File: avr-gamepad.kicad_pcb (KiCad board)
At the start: 2 copper layers, 26.2 x 48.3 mm, 33 parts, among them J1 Conn_01x08, J2 Conn_01x01, P1 USB_C_Plug_USB2.0, SW10 Up, SW11 Down, SW12 Left, SW13 Select, SW2 R, SW3 X, SW4 A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

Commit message: tweak silkscreen, add BOM
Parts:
- moved C8 0.07 mm to (140.8, 115.8), turned to 270 degrees
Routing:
- net Net-(C8-Pad1): track 2.63 -> 4.67 mm
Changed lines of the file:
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@@
     (thickness 0.1016)
     (drawings 40)
-    (tracks 455)
+    (tracks 460)
     (zones 0)
     (modules 33)
@@
     (at 151.462 125.016 180)
     (attr smd)
-    (fp_text reference SW6 (at 0 2.54) (layer F.SilkS)
+    (fp_text reference SW6 (at -0.176 2.08) (layer F.SilkS)
       (effects (font (size 1 1) (thickness 0.15)))
     )
@@
     (at 149.479 83.058 90)
     (attr smd)
-    (fp_text reference SW9 (at 0 -3.683 90) (layer B.SilkS)
+    (fp_text reference SW9 (at 3.4036 0.0254 180) (layer B.SilkS)
       (effects (font (size 1 1) (thickness 0.15)) (justify mirror))
     )
@@
     (tags capacitor)
     (attr smd)
-    (fp_text reference C1 (at 0 1.65) (layer B.SilkS)
+    (fp_text reference C1 (at -2.6876 -0.1384) (layer B.SilkS)
       (effects (font (size 1 1) (thickness 0.15)) (justify mirror))
     )
@@
     (tags capacitor)
     (attr smd)
-    (fp_text reference C2 (at 0 1.65) (layer B.SilkS)
+    (fp_text reference C2 (at -2.6876 -0.0124) (layer B.SilkS)
       (effects (font (size 1 1) (thickness 0.15)) (justify mirror))
     )
@@
     (tags capacitor)
     (attr smd)
-    (fp_text reference C3 (at 0 1.65) (layer B.SilkS)
+    (fp_text reference C3 (at -2.6576 0.0892) (layer B.SilkS)
       (effects (font (size 1 1) (thickness 0.15)) (justify mirror))
     )
@@
     (tags capacitor)
     (attr smd)
-    (fp_text reference C4 (at 0 1.65) (layer B.SilkS)
+    (fp_text reference C4 (at 0.3096 1.538) (layer B.SilkS)
       (effects (font (size 1 1) (thickness 0.15)) (justify mirror))
     )
@@
     (tags capacitor)
     (attr smd)
-    (fp_text reference C7 (at 2.667 -0.127 270) (layer B.SilkS)
+    (fp_text reference C7 (at 2.6388 0.0508 270) (layer B.SilkS)
       (effects (font (size 1 1) (thickness 0.15)) (justify mirror))
     )
@@
   )
   (module Capacitor_SMD:C_0805_2012Metric (layer B.Cu)
-    (at 140.716 115.746 90)
+    (at 140.7668 115.7963 270)
     (descr "Capacitor SMD 0805 (2012 Metric), square (rectangular) end terminal, IPC_7351 nominal, (Body size source: https://docs.google.com/spreadsheets/d/1BsfQQcO9C6DZCsRaXUlFlo91Tg2WpOkGARC1WS5S8t0/edit?usp=sharing), generated with kicad-footprint-generator")
     (tags capacitor)
     (attr smd)
-    (fp_text reference C8 (at 2.667 0 90) (layer B.SilkS)
+    (fp_text reference C8 (at 2.6693 -0.1016 90) (layer B.SilkS)
       (effects (font (size 1 1) (thickness 0.15)) (justify mirror))
     )
@@
     (fp_line (start -1 0.6) (end 1 0.6) (layer B.Fab) (width 0.1))
     (fp_line (start -1 -0.6) (end -1 0.6) (layer B.Fab) (width 0.1))
-    (pad 2 smd roundrect (at 0.9375 0 90) (size 0.975 1.4) (layers B.Cu B.Paste B.Mask) (roundrect_rratio 0.25)
-      (net 2 GND))
-    (pad 1 smd roundrect (at -0.9375 0 90) (size 0.975 1.4) (layers B.Cu B.Paste B.Mask) (roundrect_rratio 0.25)
+    (pad 2 smd roundrect (at 0.9375 0 270) (size 0.975 1.4) (layers B.Cu B.Paste B.Mask) (roundrect_rratio 0.25)
+      (net 2 GND))
+    (pad 1 smd roundrect (at -0.9375 0 270) (size 0.975 1.4) (layers B.Cu B.Paste B.Mask) (roundrect_rratio 0.25)
       (net 6 "Net-(C8-Pad1)"))
     (model ${KISYS3DMOD}/Capacitor_SMD.3dshapes/C_0805_2012Metric.wrl
@@
     (tags resistor)
     (attr smd)
-    (fp_text reference R1 (at -0.0381 -1.6891 180) (layer B.SilkS)
+    (fp_text reference R1 (at -0.1388 1.6528 180) (layer B.SilkS)
       (effects (font (size 1 1) (thickness 0.15)) (justify mirror))
     )
@@
     (tags resistor)
     (attr smd)
-    (fp_text reference R2 (at 0.079 -1.524 180) (layer B.SilkS)
+    (fp_text reference R2 (at 2.2098 0 270) (layer B.SilkS)
       (effects (font (size 1 1) (thickness 0.15)) (justify mirror))
     )
@@
     (tags resistor)
     (attr smd)
-    (fp_text reference R3 (at 0 1.5 180) (layer B.SilkS)
+    (fp_text reference R3 (at 0.5296 -1.5896 180) (layer B.SilkS)
       (effects (font (size 1 1) (thickness 0.15)) (justify mirror))
     )
@@
     (at 140.589 85.09 90)
     (attr smd)
-    (fp_text reference SW3 (at 0 3.81 90) (layer F.SilkS)
+    (fp_text reference SW3 (at -4.1148 -0.2286) (layer F.SilkS)
       (effects (font (size 1 1) (thickness 0.15)))
     )
@@
     (at 140.589 103.505)
     (attr smd)
-    (fp_text reference SW5 (at 0 3.81) (layer F.SilkS)
+    (fp_text reference SW5 (at 0 -3.8354) (layer F.SilkS)
       (effects (font (size 1 1) (thickness 0.15)))
     )
@@
     (tags "connector Hirose  top entry")
     (attr smd)
-    (fp_text reference J1 (at 0 3.7 270) (layer B.SilkS)
+    (fp_text reference J1 (at -0.0448 -1.0504 270) (layer B.SilkS)
       (effects (font (size 1 1) (thickness 0.15)) (justify mirror))
     )
@@
   (segment (start 138.1825 120.6933) (end 141.8278 117.048) (width 0.3048) (layer B.Cu) (net 2))
   (segment (start 141.8278 117.048) (end 141.8278 116.7135) (width 0.3048) (layer B.Cu) (net 2))
-  (segment (start 141.8278 116.7135) (end 141.8278 116.3179) (width 0.3048) (layer B.Cu) (net 2))
-  (segment (start 141.8278 116.3179) (end 141.2559 115.746) (width 0.3048) (layer B.Cu) (net 2))
-  (segment (start 140.716 114.8085) (end 141.2559 115.3484) (width 0.3048) (layer B.Cu) (net 2))
-  (segment (start 141.2559 115.3484) (end 141.2559 115.746) (width 0.3048) (layer B.Cu) (net 2))
   (segment (start 141.072 115.6111) (end 139.6271 117.056) (width 0.3048) (layer F.Cu) (net 2))
   (segment (start 141.072 112.156) (end 141.072 115.6111) (width 0.3048) (layer F.Cu) (net 2))
-  (segment (start 141.2559 115.746) (end 141.2069 115.746) (width 0.3048) (layer F.Cu) (net 2))
-  (segment (start 141.2069 115.746) (end 141.072 115.6111) (width 0.3048) (layer F.Cu) (net 2))
   (segment (start 138.049 88.3321) (end 139.1997 88.3321) (width 0.3048) (layer B.Cu) (net 2))
   (segment (start 139.1997 88.3321) (end 146.939 96.0714) (width 0.3048) (layer B.Cu) (net 2))
@@
   (segment (start 128.5 109.925) (end 129.1907 109.925) (width 0.3048) (layer F.Cu) (net 2))
   (via (at 146.939 79.9448) (size 0.508) (layers F.Cu B.Cu) (net 2))
-  (via (at 141.2559 115.746) (size 0.508) (layers F.Cu B.Cu) (net 2))
   (via (at 138.049 88.3321) (size 0.508) (layers F.Cu B.Cu) (net 2))
   (via (at 138.049 108.8708) (size 0.508) (layers F.Cu B.Cu) (net 2))
@@
   (via (at 145.3488 118.217) (size 0.508) (layers F.Cu B.Cu) (net 2))
   (via (at 129.4372 109.7357) (size 0.508) (layers F.Cu B.Cu) (net 2))
+  (segment (start 141.8075 116.7338) (end 141.8278 116.7135) (width 0.3048) (layer B.Cu) (net 2))
+  (segment (start 140.7668 116.7338) (end 141.8075 116.7338) (width 0.3048) (layer B.Cu) (net 2))
+  (via (at 141.681198 115.824) (size 0.508) (drill 0.254) (layers F.Cu B.Cu) (net 2))
+  (segment (start 141.681198 116.566898) (end 141.681198 116.18321) (width 0.3048) (layer B.Cu) (net 2))
+  (segment (start 141.681198 116.18321) (end 141.681198 115.824) (width 0.3048) (layer B.Cu) (net 2))
+  (segment (start 141.8278 116.7135) (end 141.681198 116.566898) (width 0.3048) (layer B.Cu) (net 2))
+  (segment (start 141.321988 115.824) (end 141.681198 115.824) (width 0.3048) (layer F.Cu) (net 2))
+  (segment (start 141.072 115.6111) (end 141.2849 115.824) (width 0.3048) (layer F.Cu) (net 2))
+  (segment (start 141.2849 115.824) (end 141.321988 115.824) (width 0.3048) (layer F.Cu) (net 2))
   (segment (start 144.272 122.5771) (end 144.272 122.1269) (width 0.1524) (layer F.Cu) (net 3))
   (segment (start 144.272 122.1269) (end 146.4474 119.9515) (width 0.1524) (layer F.Cu) (net 3))
@@
   (segment (start 141.872 112.156) (end 141.872 113.1349) (width 0.1524) (layer F.Cu) (net 5))
   (via (at 141.872 113.9625) (size 0.508) (layers F.Cu B.Cu) (net 5))
-  (segment (start 139.5509 117.856) (end 139.7407 117.6662) (width 0.1524) (layer F.Cu) (net 6))
-  (segment (start 139.7407 117.6662) (end 139.7407 117.6588) (width 0.1524) (layer F.Cu) (net 6))
-  (segment (start 140.716 116.6835) (end 139.7407 117.6588) (width 0.1524) (layer B.Cu) (net 6))
-  (segment (start 138.572 117.856) (end 139.5509 117.856) (width 0.1524) (layer F.Cu) (net 6))
-  (via (at 139.7407 117.6588) (size 0.508) (layers F.Cu B.Cu) (net 6))
+  (via (at 139.8524 117.8052) (size 0.508) (drill 0.254) (layers F.Cu B.Cu) (net 6))
+  (segment (start 138.572 117.856) (end 139.8016 117.856) (width 0.1524) (layer F.Cu) (net 6))
+  (segment (start 139.8016 117.856) (end 139.8524 117.8052) (width 0.1524) (layer F.Cu) (net 6))
+  (segment (start 140.210563 115.415037) (end 140.7668 114.8588) (width 0.1524) (layer B.Cu) (net 6))
+  (segment (start 139.8016 115.824) (end 140.210563 115.415037) (width 0.1524) (layer B.Cu) (net 6))
+  (segment (start 139.8016 117.39519) (end 139.8016 115.824) (width 0.1524) (layer B.Cu) (net 6))
+  (segment (start 139.8524 117.8052) (end 139.8524 117.44599) (width 0.1524) (layer B.Cu) (net 6))
+  (segment (start 139.8524 117.44599) (end 139.8016 117.39519) (width 0.1524) (layer B.Cu) (net 6))
   (segment (start 149.3825 106.172) (end 149.3525 106.202) (width 0.1524) (layer F.Cu) (net 7))
   (segment (start 149.3525 106.202) (end 149.3525 108.712) (width 0.1524) (layer F.Cu) (net 7))

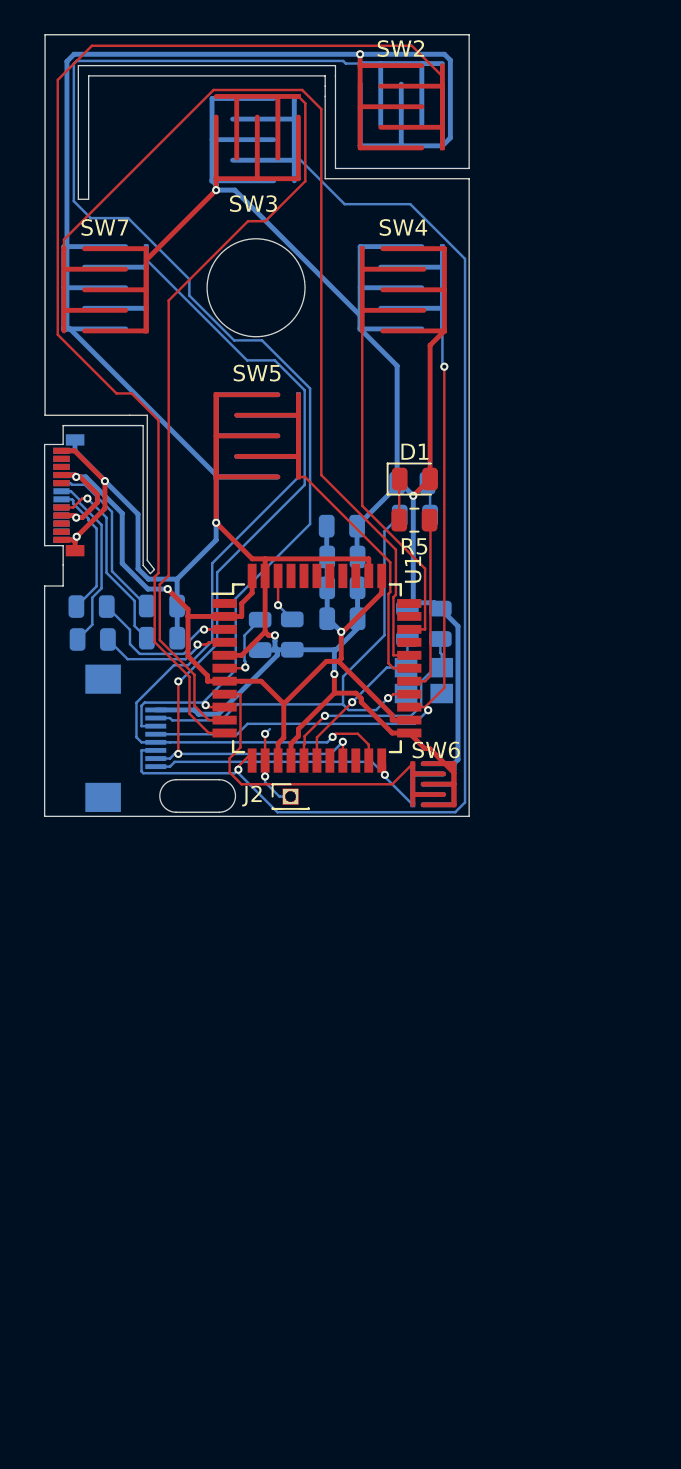
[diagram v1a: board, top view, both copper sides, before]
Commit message: begin v2. Remove flex, move components to one side, expand board size, remove excess caps, recess usb connector
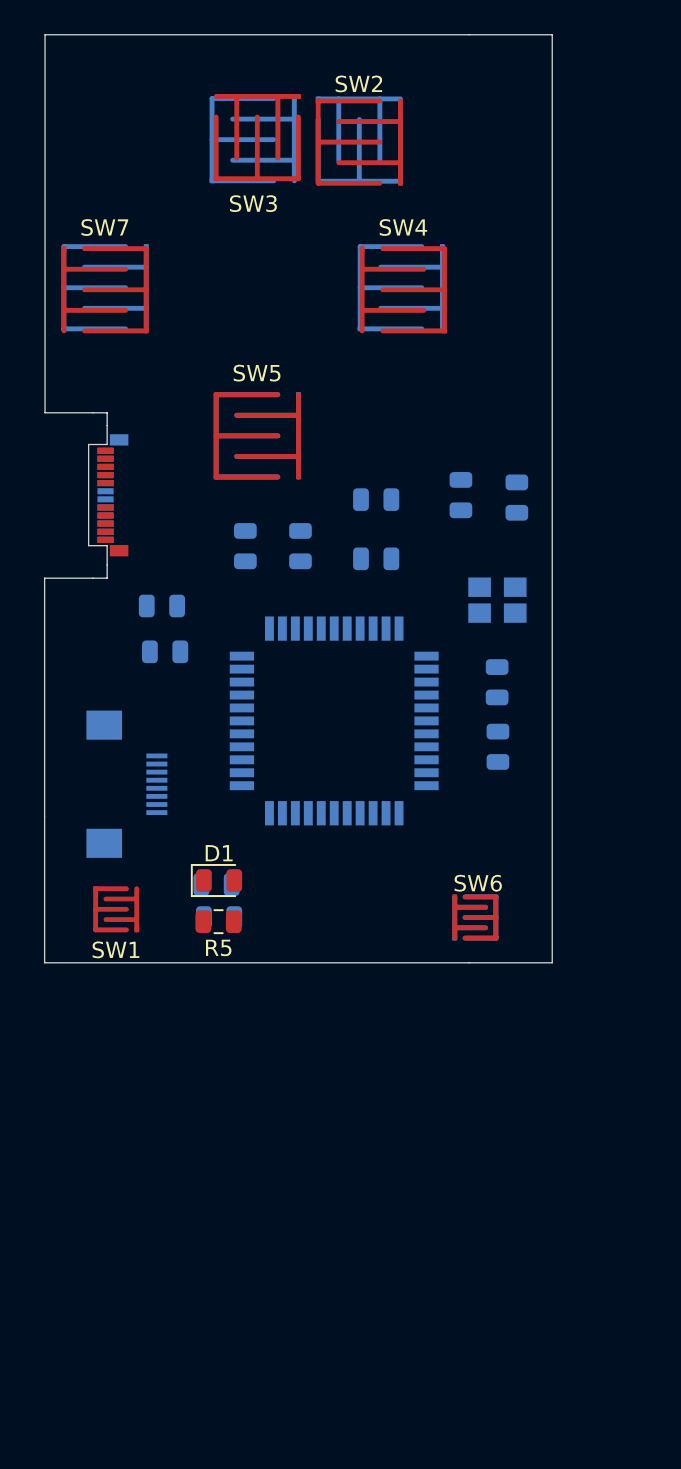
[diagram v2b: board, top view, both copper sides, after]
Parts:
- removed C2, C3: 0.1uF, Capacitor_SMD:C_0805_2012Metric
- removed J2: Conn_01x01, Connector_PinHeader_1.27mm:PinHeader_1x01_P1.27mm_Vertical
- added SW1: SW_Push, Button Contacts:Contact2, F.Cu at (131.9, 132.7)
- U1: moved to B.Cu
- moved D1 27.6 mm to (138.2, 131.0)
- moved R6 27.6 mm to (138.2, 133.2)
- moved D2 27.6 mm to (138.1, 131.2)
- moved R5 27.6 mm to (138.2, 133.5)
- moved R2 25.9 mm to (155.4, 122.7), turned to 270 degrees
- moved R4 25.5 mm to (155.4, 118.7), turned to 90 degrees
- moved C6 9.11 mm to (156.6, 107.3)
- moved SW13 8.63 mm to (154.1, 133.2)
- moved SW6 8.63 mm to (154.1, 133.2)
- moved C5 8.60 mm to (153.2, 107.2)
- moved Y1 6.73 mm to (155.4, 113.7)
- moved C8 5.56 mm to (139.9, 110.3)
- moved C7 5.49 mm to (143.3, 110.3)
- moved C4 4.24 mm to (147.9, 111.1)
- moved C1 4.11 mm to (147.9, 107.4)
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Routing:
- net GND: track 235.0 -> 0.00 mm, vias 8 -> 0
- net /pb1: track 75.9 -> 0.00 mm, vias 1 -> 0
- net /pb7: track 75.9 -> 0.00 mm, vias 1 -> 0
- net /pb3: track 75.7 -> 0.00 mm
- net +5V: track 63.8 -> 0.00 mm, vias 4 -> 0
- net /pb5: track 57.4 -> 0.00 mm
- net /pd1: track 52.8 -> 0.00 mm, vias 3 -> 0
- net /pd4: track 47.7 -> 0.00 mm, vias 2 -> 0
- net /pb2: track 45.3 -> 0.00 mm
- net /pd3: track 41.8 -> 0.00 mm, vias 1 -> 0
- net /pd6: track 29.8 -> 0.00 mm, vias 1 -> 0
- net /pc6: track 26.1 -> 0.00 mm
- net /pb0: track 18.2 -> 0.00 mm
- net /pd5: track 18.1 -> 0.00 mm, vias 1 -> 0
- net /pb4: track 15.5 -> 0.00 mm
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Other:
- board size 26.2 x 48.3 mm -> 31.3 x 57.3 mm

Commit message: change main pad shape, shuffle things
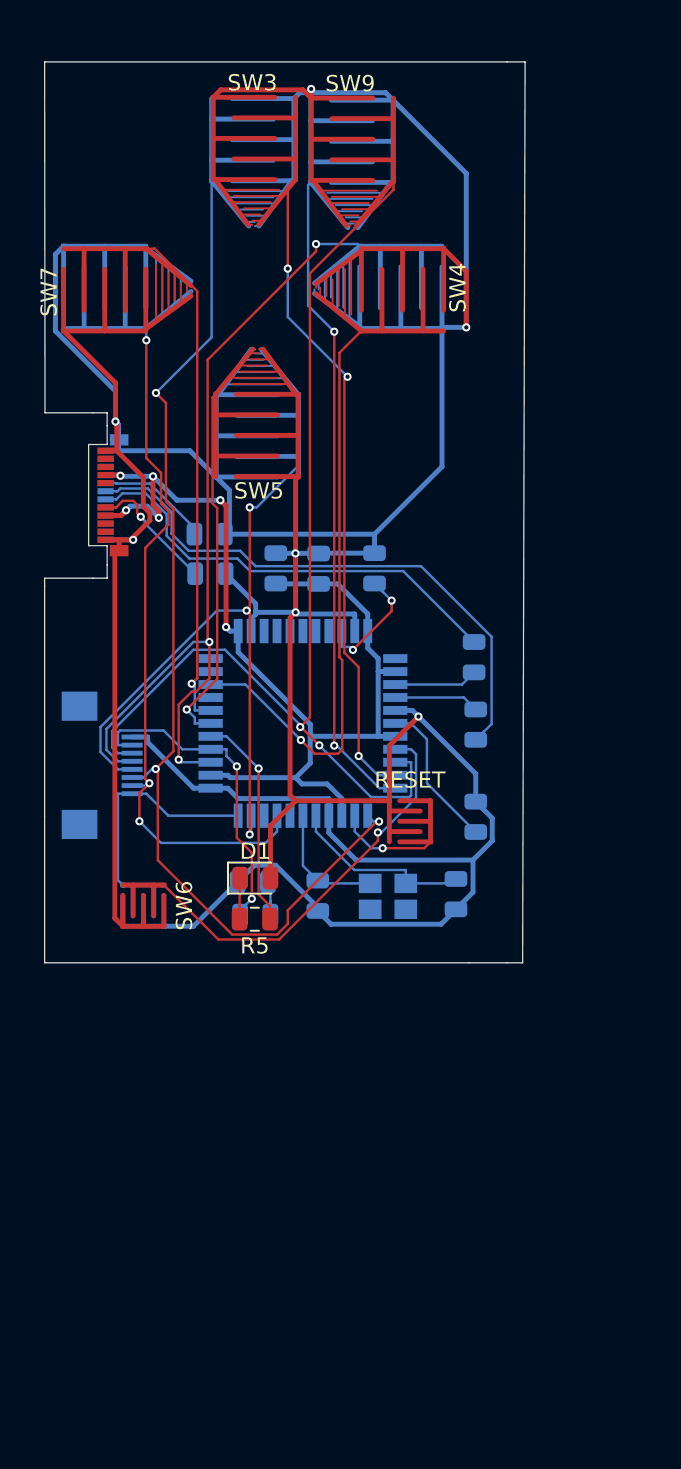
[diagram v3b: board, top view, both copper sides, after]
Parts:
- removed SW1: SW_Push, Button Contacts:Contact2
- added RESET: RESET, Button Contacts:Small, F.Cu at (150.0, 127.3)
- SW10, SW11, SW12, SW3, SW4, SW5, SW7, SW8: footprint Button Contacts:Contact1 -> Button Contacts:Large_tapered
- SW13, SW6: footprint Button Contacts:Contact2 -> Button Contacts:Small
- SW2: footprint Button Contacts:Contact1 -> Button Contacts:Large_tapered; moved to B.Cu
- SW9: footprint Button Contacts:Contact1 -> Button Contacts:Large_tapered; moved to F.Cu
- moved C5 26.3 mm to (144.3, 131.9), turned to 270 degrees
- moved C6 24.8 mm to (152.9, 131.8), turned to 270 degrees
- moved C8 21.9 mm to (154.1, 127.0), turned to 90 degrees
- moved SW13 20.5 mm to (133.6, 132.5), turned to 90 degrees
- moved SW6 20.5 mm to (133.6, 132.5), turned to 90 degrees
- moved Y1 19.5 mm to (148.7, 131.9)
- moved C1 7.51 mm to (141.7, 111.7), turned to 90 degrees
- moved R1 5.58 mm to (137.7, 112.0)
- moved R3 5.32 mm to (137.6, 109.6)
- moved C7 4.77 mm to (147.8, 111.7), turned to 90 degrees
- moved C4 3.61 mm to (144.4, 111.7), turned to 90 degrees
- moved D1 2.24 mm to (140.5, 130.8)
- moved D2 2.24 mm to (140.3, 131.1)
- moved R5 2.24 mm to (140.4, 133.3)
- moved R6 2.24 mm to (140.5, 133.1)
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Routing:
- net GND: track 0.00 -> 250.8 mm, vias 0 -> 7
- net +5V: track 0.00 -> 67.1 mm, vias 0 -> 6
- net /pb1: track 0.00 -> 66.0 mm, vias 0 -> 2
- net /pb7: track 0.00 -> 65.8 mm, vias 0 -> 3
- net /pd4: track 0.00 -> 52.1 mm, vias 0 -> 3
- net /pd3: track 0.00 -> 46.0 mm, vias 0 -> 3
- net /pd1: track 0.00 -> 43.4 mm, vias 0 -> 3
- net /pb2: track 0.00 -> 40.5 mm, vias 0 -> 3
- net /pb3: track 0.00 -> 40.4 mm, vias 0 -> 2
- net /pc6: track 0.00 -> 36.5 mm, vias 0 -> 1
- net Net-(P1-PadA6): track 0.00 -> 35.9 mm
- net /pb5: track 0.00 -> 31.3 mm, vias 0 -> 1
- net Net-(P1-PadA7): track 0.00 -> 27.5 mm
- net /pb0: track 0.00 -> 25.0 mm, vias 0 -> 1
- net /pb4: track 0.00 -> 22.5 mm, vias 0 -> 1
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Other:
- board size 31.3 x 57.3 mm -> 29.7 x 55.6 mm
